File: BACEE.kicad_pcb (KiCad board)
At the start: 2 copper layers, 43.4 x 29.7 mm, 17 parts, among them J1 Serial, J2 Digital pins, J3 ICSP, J4 I2C, U1 24LC1025, U2 24LC1025, U3 DS1337_KTH, U4 ATMEGA328P-AU, Y1 Crystal 32MHz, Y2 Crystal 16MHz

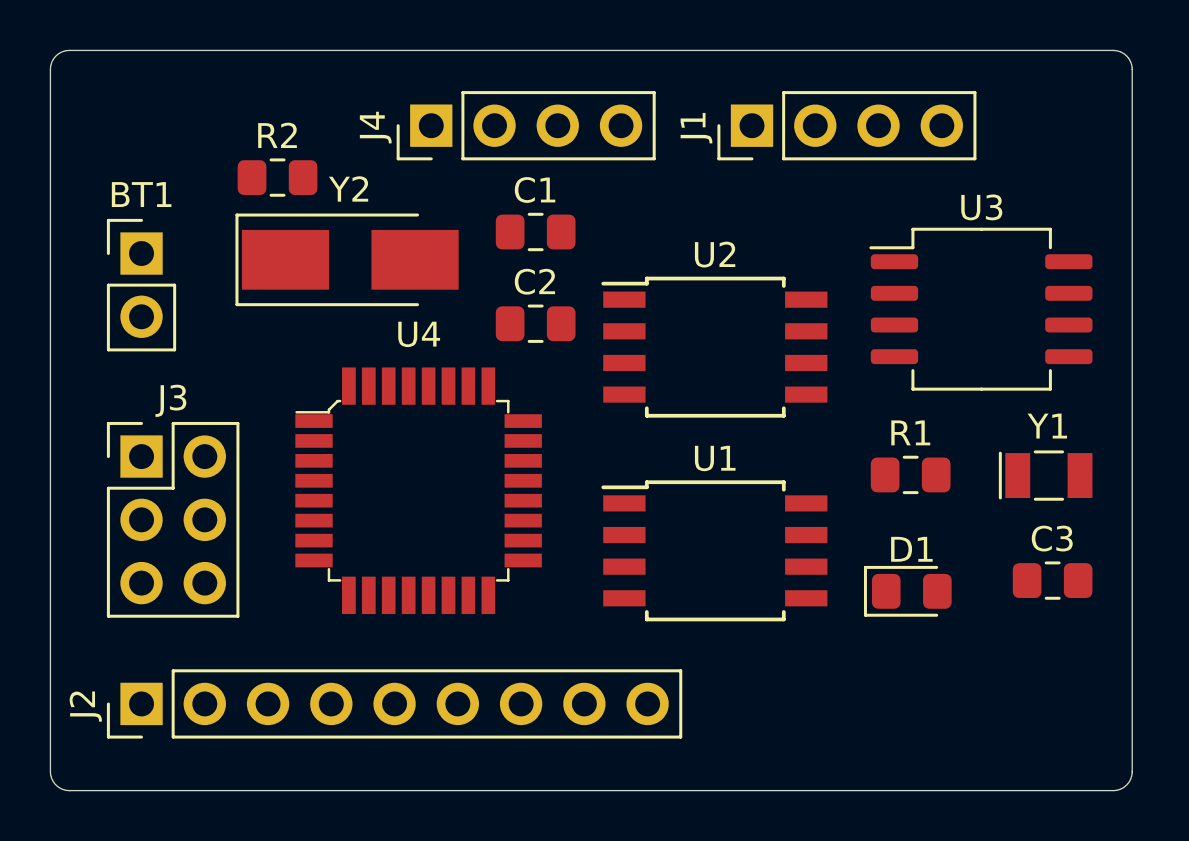
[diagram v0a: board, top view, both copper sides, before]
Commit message: board layout with mounting holes
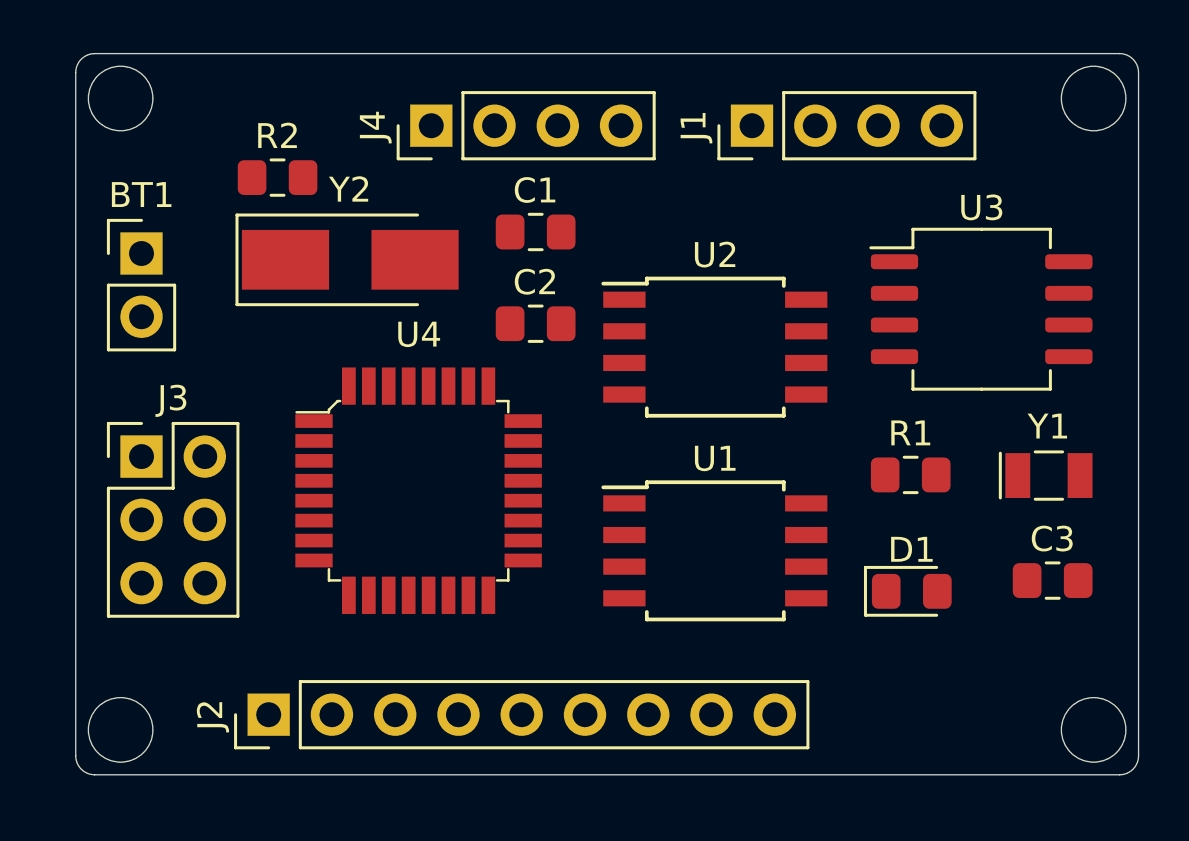
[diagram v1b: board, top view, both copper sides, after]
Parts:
- moved J2 5.12 mm to (93.3, 135.4)
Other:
- board size 43.4 x 29.7 mm -> 42.7 x 29 mm
